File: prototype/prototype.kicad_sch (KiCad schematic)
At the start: 86 parts, among them J1 XT60, J10 XT30, J11 XT30, J12 XT30, J13 XT30, J14 JST_XH_4P, J15 JST_XH_4P, J16 Switch, J17 IMU_JST_XH_4P, J18 BT_UART, J19 JST_XH_4P, J2 XT60, J3 Conn_01x20_Pin, J4 Conn_01x20_Pin, J5 Conn_01x03_Pin, J6 JST_XH_3P, J7 Conn_01x01_Pin, J8 JST_XH_01x02, J9 JST_XH_01x02, M1 Mouse Hole, M10 Mouse Hole, M11 Mouse Hole, M13 Mouse Hole, M14 Mouse Hole, M15 Mouse Hole, M16 Mouse Hole, M17 Mouse Hole, M18 Mouse Hole, M19 Mouse Hole, M2 Mouse Hole, M20 Mouse Hole, M21 Mouse Hole, M22 Mouse Hole, M23 Mouse Hole, M24 Mouse Hole, M25 Mouse Hole, M26 Mouse Hole, M27 Mouse Hole, M28 Mouse Hole, M29 Mouse Hole, M3 Mouse Hole, M30 Mouse Hole, M31 Mouse Hole, M32 Mouse Hole, M33 Mouse Hole, M34 Mouse Hole, M35 Mouse Hole, M36 Mouse Hole, M37 Mouse Hole, M38 Mouse Hole, M39 Mouse Hole, M4 Mouse Hole, M40 Mouse Hole, M5 Mouse Hole, M6 Mouse Hole, M7 Mouse Hole, M8 Mouse Hole, M9 Mouse Hole, U1 Raspberry-Pi-Pico

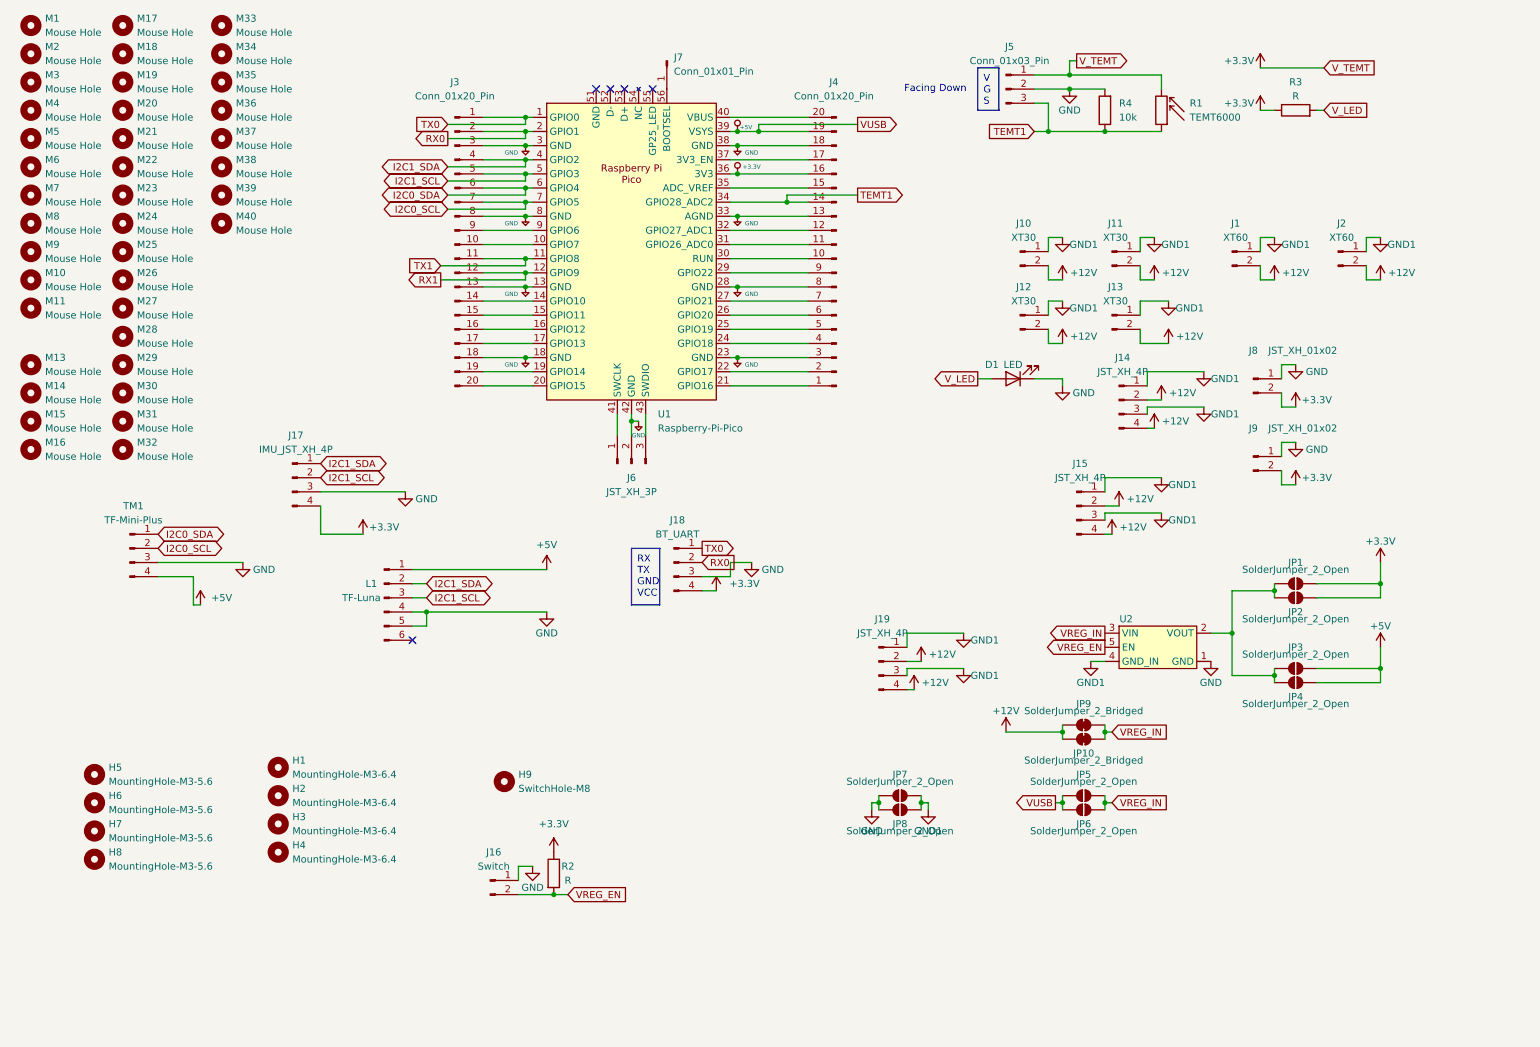
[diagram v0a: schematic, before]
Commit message: pcbs: feat: updated schematics with pdf
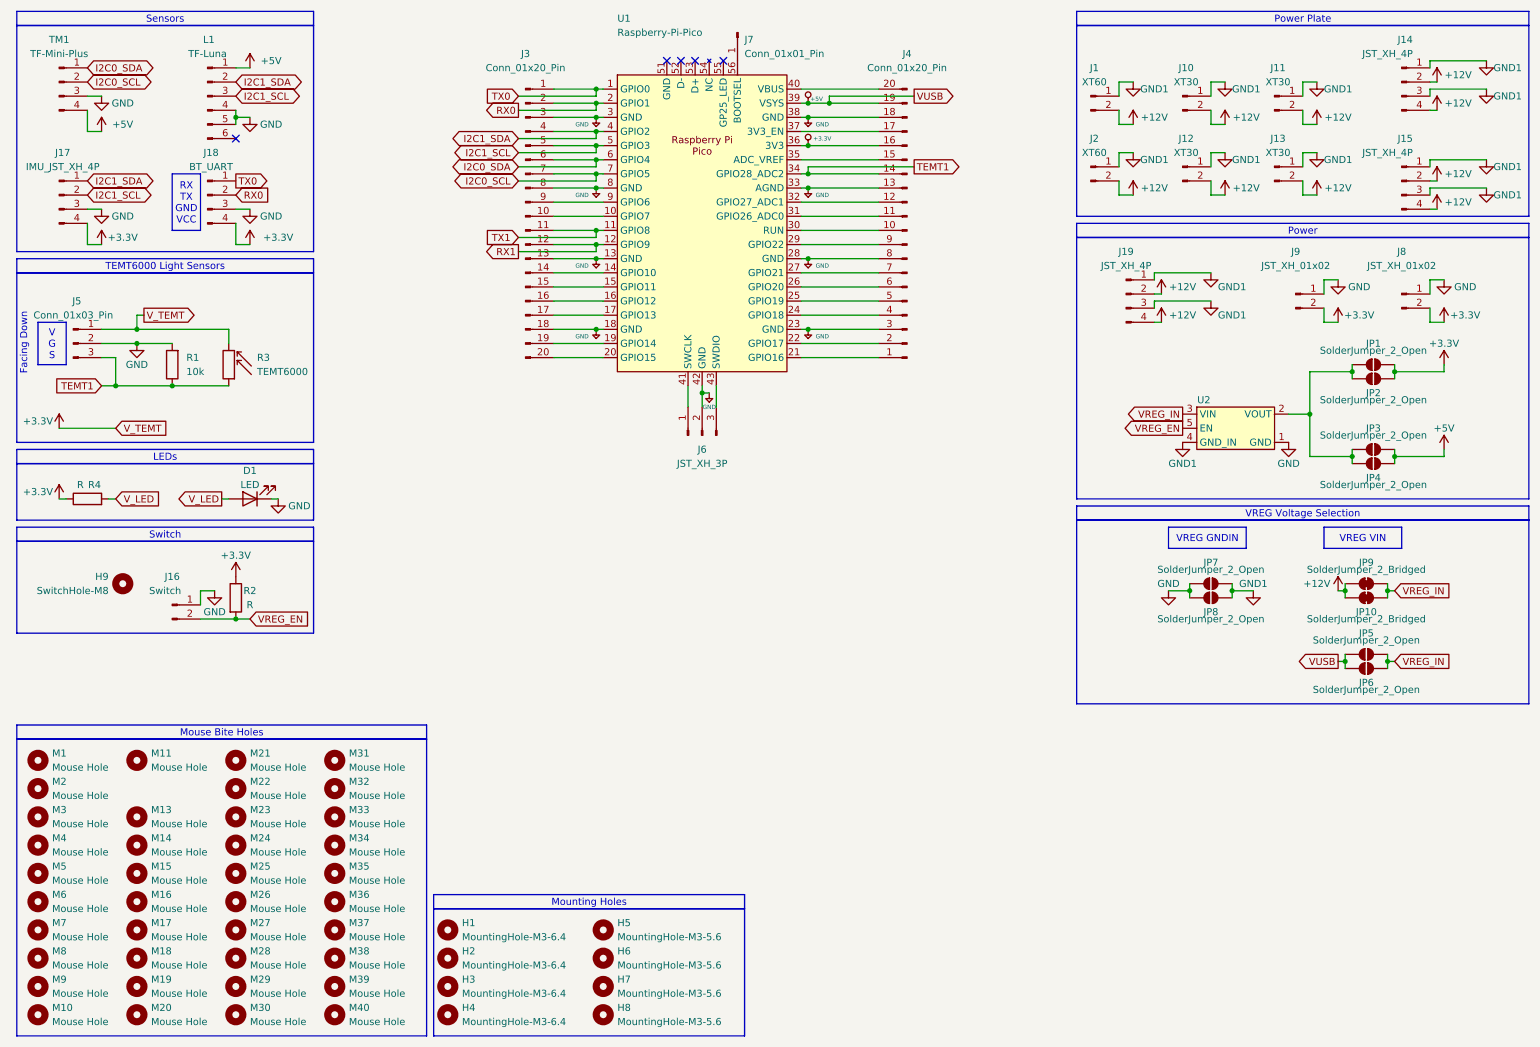
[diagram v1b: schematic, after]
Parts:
- removed R1: TEMT6000, PorridgePi-Personal:TEMT6000-SMD, symbol Device:R_Photo
- removed R3: R, PCM_Resistor_THT_AKL:R_Box_L8.4mm_W2.5mm_P5.08mm, symbol Device:R
- added R1: 10k, Resistor_SMD:R_0603_1608Metric_Pad0.98x0.95mm_HandSolder, symbol Device:R
- added R3: TEMT6000, PorridgePi-Personal:TEMT6000-SMD, symbol Device:R_Photo
- R4: value 10k -> R; footprint Resistor_SMD:R_0603_1608Metric_Pad0.98x0.95mm_HandSolder -> PCM_Resistor_THT_AKL:R_Box_L8.4mm_W2.5mm_P5.08mm
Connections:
- net +3.3V: now also R4.1, R3.2
- net GND: now also R1.2; no longer R4.2
- net TEMT1: now also R1.1, R3.1; no longer R4.1
- net V_LED: now also R4.2
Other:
- moved on the sheet: H1, H2, H3, H4, H5, H6, H7, H8, H9, J1, J10, J11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
